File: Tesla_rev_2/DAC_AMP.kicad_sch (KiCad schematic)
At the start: 39 parts, among them K1 G6EU, Q3 BC817, Q4 BC817, U5 MCP6497, U6 PCM5102A, U7 TPA0211

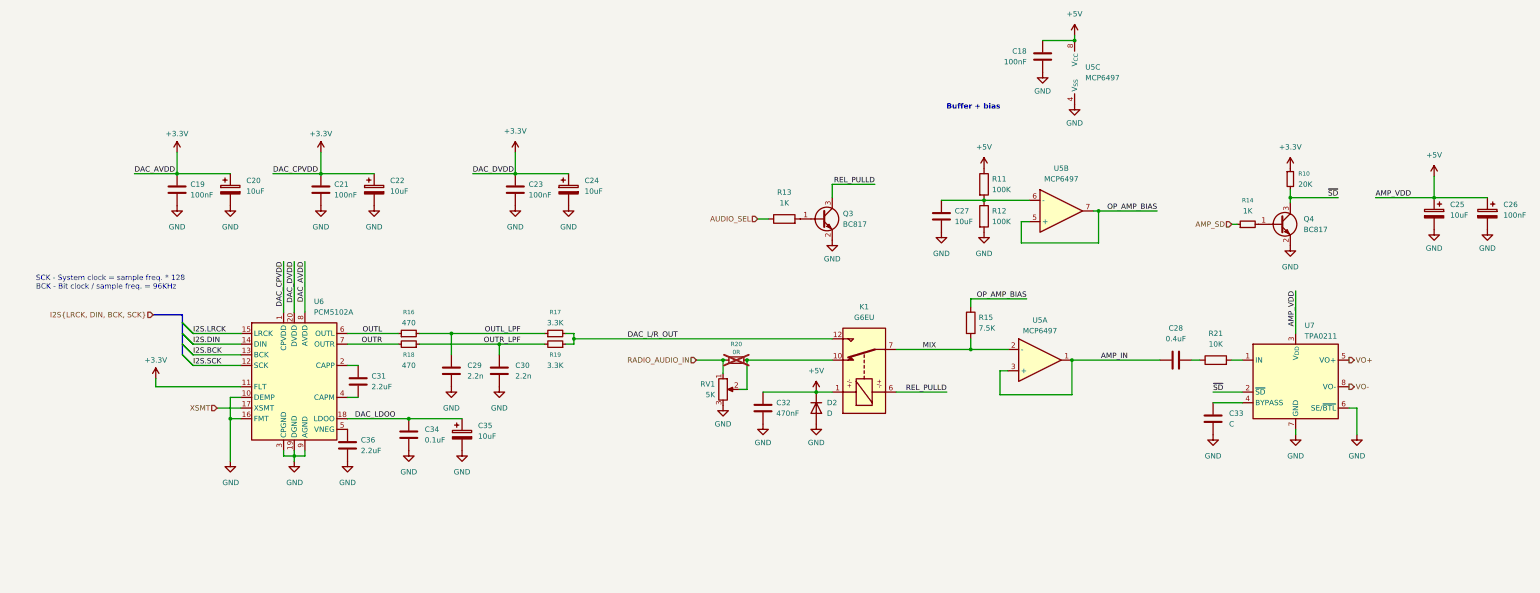
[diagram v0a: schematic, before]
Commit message: Netclasses, part Nums, LPF adjust
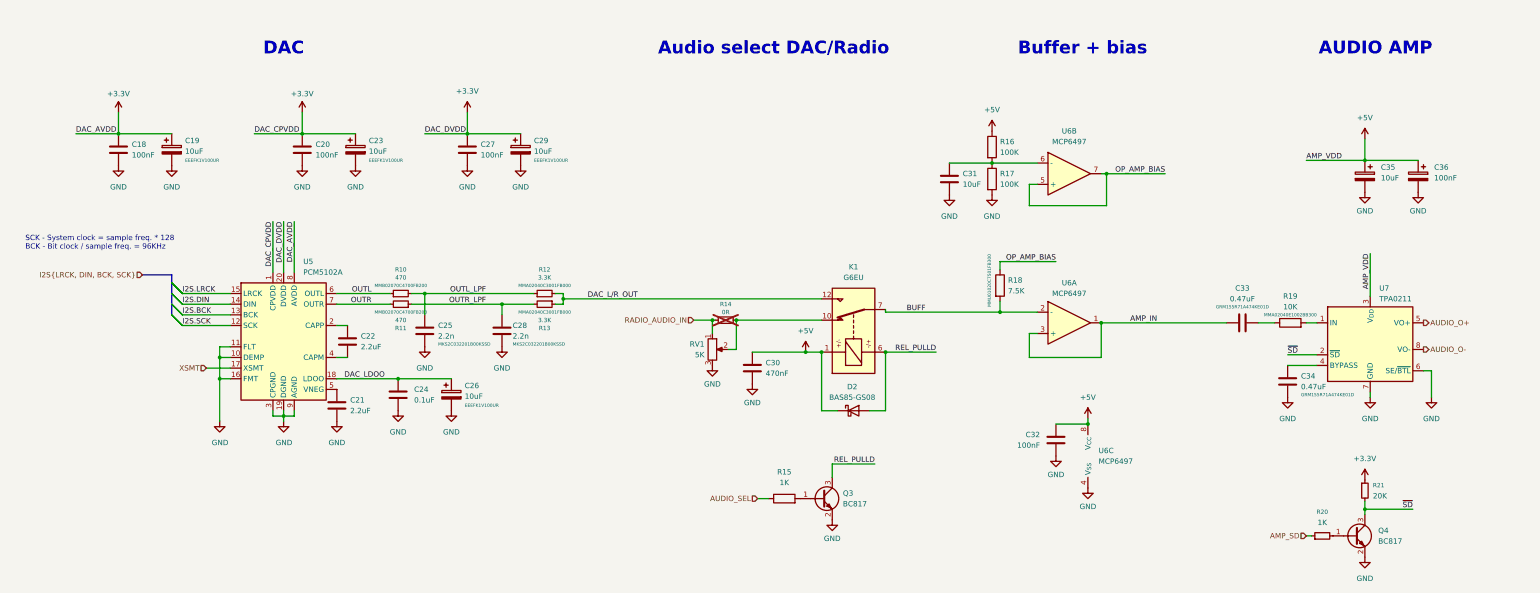
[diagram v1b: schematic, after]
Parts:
- removed C20, C22, C24, C35: 10uF, Capacitor_SMD:CP_Elec_6.3x7.7, symbol Device:C_Polarized
- removed C30: 2.2n, symbol Device:C
- removed D2: D, symbol Device:D
- removed R18: 470, symbol Device:R_Small
- removed R19: 3.3K, symbol Device:R_Small
- added C19, C23, C26, C29: 10uF, symbol Device:C_Polarized
- added C33: 0.47uF, symbol Device:C
- added D2: BAS85-GS08, Diode_SMD:D_MiniMELF, symbol Device:D_Schottky
- added R11: 470, symbol Device:R_Small
- added R13: 3.3K, symbol Device:R_Small
- C25: renamed from C29; Part_num (none) -> MKS2C032201B00KSSD
- C28: value 0.4uF -> 2.2n; Part_num (none) -> MKS2C032201B00KSSD
- C34: renamed from C33; value C -> 0.47uF; Part_num (none) -> GRM155R71A474KE01D
- R10: renamed from R16; Part_num (none) -> MMB02070C4700FB200
- R12: renamed from R17; Part_num (none) -> MMA02040C3001FB000
- R18: renamed from R15; Part_num (none) -> MMU01020C7501FB300
- R19: renamed from R21; Part_num (none) -> MMA02040E1002BB300
- renumbered C19 to C18, C21 to C20, C36 to C21, C31 to C22, C34 to C24, C23 to C27, C32 to C30, C27 to C31, C18 to C32, C25 to C35, C26 to C36, R20 to R14, R13 to R15, R11 to R16, R12 to R17, R14 to R20, R10 to R21, U6 to U5, U5 to U6
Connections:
- net +3.3V: now also C19.1, C23.1, C29.1; no longer U5.11 (FLT)
- net +5V: now also D2.1 (K)
- net AMP_IN: now also C33.1; no longer C28.1
- net DAC_LDOO: now also C26.1
- net DAC_L/R_OUT: now also R13.1
- net GND: now also C28.2, U5.11 (FLT), C19.2, C23.2, C26.2, C29.2
- net OUTR: now also R11.2
- net OUTR_LPF: now also C28.1, R11.1, R13.2
- net REL_PULLD: now also D2.2 (A)
- net at R19.1: now also C33.2; no longer C28.2
- net MIX renamed BUFF
- net VO+ renamed AUDIO_O+
- net VO- renamed AUDIO_O-
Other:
- note added: "AUDIO AMP"
- note added: "Audio select DAC/Radio"
- note added: "DAC"
- title: (none) -> Tesla sextant BT
- moved on the sheet: C18, C20, C21, C22, C24, C25, C27, C30, C31, C32, C34, C35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
